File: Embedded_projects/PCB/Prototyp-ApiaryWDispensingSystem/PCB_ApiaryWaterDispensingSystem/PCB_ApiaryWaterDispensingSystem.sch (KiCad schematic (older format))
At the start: 0 parts

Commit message: added lot of changes to project #3
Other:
- note added: "Future"
- note added: "Ready"
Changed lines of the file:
@@
 $Descr A4 11693 8268
 encoding utf-8
-Sheet 1 7
+Sheet 1 9
 Title ""
 Date ""
@@
 $EndDescr
 $Sheet
-S 1180 1410 1050 1450
+S 4650 3150 1270 1660
 U 67C77D26
 F0 "Microcontroller_F4" 50
 F1 "microcontroller_F4.sch" 50
+F2 "SWO" B R 5920 4170 50
+F3 "USART_TX" O R 5920 4360 50
+F4 "USART_RX" I R 5920 4440 50
+F5 "TMS" B R 5920 4100 50
+F6 "TCK" B R 5920 4030 50
+F7 "MCO" B R 5920 4670 50
+F8 "NRST" B R 5920 4740 50
+F9 "BOOT0" B R 5920 4600 50
+F10 "SCL" B L 4650 4680 50
+F11 "SDA" B L 4650 4610 50
+F12 "B1_Button" O L 4650 3740 50
+F13 "B2_Button" O L 4650 3820 50
+F14 "B3_Button" O L 4650 3900 50
+F15 "B4_Button" O L 4650 3980 50
+F16 "SPI3_MOSI" O L 4650 3290 50
+F17 "SPI3_MISO" O L 4650 3360 50
+F18 "SPI3_CS" O L 4650 3440 50
+F19 "SPI3_SCK" O L 4650 3520 50
+F20 "APHASE" O R 5920 3300 50
+F21 "AENABLE" O R 5920 3370 50
+F22 "MODE" O R 5920 3450 50
 $EndSheet
 $Sheet
-S 5650 2000 1450 1350
+S 9410 1420 1450 1350
 U 67C77F5E
 F0 "MPPT" 50
@@
 $EndSheet
 $Sheet
-S 4200 3750 1100 1200
+S 2730 4410 1100 1200
 U 67D47B32
 F0 "sensors" 50
 F1 "sensors.sch" 50
-F2 "SDA" B L 4200 3950 50
-F3 "SCL" B L 4200 4050 50
+F2 "SDA" B R 3830 4610 50
+F3 "SCL" B R 3830 4680 50
+F4 "RST" B R 3830 5150 50
+F5 "BH_I2C_ADDR" B R 3830 5260 50
 $EndSheet
 $Sheet
-S 6100 3850 1150 1100
+S 6440 3100 1120 630
 U 67E19E2D
 F0 "sterownik_silnika" 50
 F1 "sterownik_silnika.sch" 50
-F2 "APHASE" I L 6100 4050 50
-F3 "BPHASE" I L 6100 4140 50
-F4 "AENBL" I L 6100 4230 50
-F5 "BENBL" I L 6100 4320 50
-F6 "MODE" I L 6100 4390 50
+F2 "APHASE" I L 6440 3300 50
+F3 "BPHASE" I L 6440 3510 50
+F4 "AENBL" I L 6440 3370 50
+F5 "BENBL" I L 6440 3580 50
+F6 "MODE" I L 6440 3440 50
 $EndSheet
 $Sheet
-S 7670 2200 1170 1120
+S 3220 2960 650  710
 U 67E3C70E
 F0 "SPI" 50
 F1 "SPI.sch" 50
+F2 "SPI3_SCK" I R 3870 3520 50
+F3 "SPI3_MOSI" I R 3870 3290 50
+F4 "SPI3_MISO" I R 3870 3360 50
+F5 "SPI3_CS" I R 3870 3440 50
 $EndSheet
 $Sheet
-S 3090 1680 900  1070
+S 7980 4040 970  510
+U 67F92507
+F0 "Zasilanie" 50
+F1 "Zasilanie.sch" 50
+F2 "PWR_ENn" I L 7980 4290 50
+$EndSheet
+Text Notes 9470 1070 0    157  ~ 0
+Future
+Text Notes 6670 3710 0    50   ~ 0
+Ready
+Text Notes 9810 1240 0    50   ~ 0
+Ready
+Wire Wire Line
+	4650 3290 3870 3290
+Wire Wire Line
+	3870 3360 4650 3360
+Wire Wire Line
+	3870 3440 4650 3440
+Wire Wire Line
+	3870 3520 4650 3520
+Wire Wire Line
+	3830 4610 4650 4610
+Wire Wire Line
+	4650 4680 3830 4680
+Wire Wire Line
+	7980 4290 7380 4290
+$Sheet
+S 1330 3540 800  620
+U 6823454A
+F0 "Buttons" 50
+F1 "Buttons.sch" 50
+F2 "UP_BUTTON" I R 2130 3740 50
+F3 "DOWN_BUTTON" I R 2130 3820 50
+F4 "ACTIVATED_BUTTON" I R 2130 3900 50
+F5 "OPTION_BUTTON" I R 2130 3980 50
+$EndSheet
+Wire Wire Line
+	4650 3740 2130 3740
+Wire Wire Line
+	2130 3820 4650 3820
+Wire Wire Line
+	4650 3900 2130 3900
+Wire Wire Line
+	2130 3980 4650 3980
+$Sheet
+S 6430 3920 900  1070
 U 6818B51C
 F0 "Microcontroller_F1" 50
 F1 "Microcontroller_F1.sch" 50
-F2 "STLK_TX" O L 3090 2280 50
-F3 "STLK_RX" I L 3090 2210 50
-F4 "MCO" U L 3090 2350 50
-F5 "PWR_ENn" O L 3090 2570 50
-F6 "NRST" O L 3090 1930 50
-F7 "TCK" O L 3090 2000 50
-F8 "TMS" O L 3090 2070 50
-F9 "SWO" O L 3090 2140 50
+F2 "STLK_TX" O L 6430 4530 50
+F3 "STLK_RX" I L 6430 4450 50
+F4 "MCO" U L 6430 4650 50
+F5 "PWR_ENn" O R 7330 4170 50
+F6 "NRST" O L 6430 4730 50
+F7 "TCK" O L 6430 4170 50
+F8 "TMS" O L 6430 4240 50
+F9 "SWO" O L 6430 4300 50
 $EndSheet
+Wire Wire Line
+	6440 3300 5920 3300
+Wire Wire Line
+	5920 3370 6440 3370
+Wire Wire Line
+	6440 3440 5950 3440
+Wire Wire Line
+	5950 3440 5950 3450
+Wire Wire Line
+	5950 3450 5920 3450
+Wire Wire Line
+	5920 4030 6220 4030
+Wire Wire Line
+	6220 4030 6220 4170
+Wire Wire Line
+	6220 4170 6430 4170
+Wire Wire Line
+	5920 4100 6160 4100
+Wire Wire Line
+	6160 4100 6160 4240
+Wire Wire Line
+	6160 4240 6430 4240
+Wire Wire Line
+	5920 4170 6100 4170
+Wire Wire Line
+	6100 4170 6100 4300
+Wire Wire Line
+	6100 4300 6430 4300
+Wire Wire Line
+	5920 4360 6250 4360
+Wire Wire Line
+	6250 4360 6250 4450
+Wire Wire Line
+	6250 4450 6430 4450
+Wire Wire Line
+	5920 4440 6180 4440
+Wire Wire Line
+	6180 4440 6180 4530
+Wire Wire Line
+	6180 4530 6430 4530
+Wire Wire Line
+	5920 4670 6340 4670
+Wire Wire Line
+	6340 4670 6340 4650
+Wire Wire Line
+	6340 4650 6430 4650
+Wire Wire Line
+	6430 4730 6170 4730
+Wire Wire Line
+	5960 4730 5960 4740
+Wire Wire Line
+	5960 4740 5920 4740
+Wire Wire Line
+	3830 5150 6170 5150
+Wire Wire Line
+	6170 5150 6170 4730
+Connection ~ 6170 4730
+Wire Wire Line
+	6170 4730 5960 4730
 $EndSCHEMATC

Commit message: Many design changes have been added over the past few months #3
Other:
- note added: "good"
- note removed: "Future"
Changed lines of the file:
@@
 $EndDescr
 $Sheet
-S 4650 3150 1270 1660
+S 4650 3150 1270 2080
 U 67C77D26
 F0 "Microcontroller_F4" 50
@@
 F5 "TMS" B R 5920 4100 50
 F6 "TCK" B R 5920 4030 50
-F7 "MCO" B R 5920 4670 50
-F8 "NRST" B R 5920 4740 50
-F9 "BOOT0" B R 5920 4600 50
-F10 "SCL" B L 4650 4680 50
-F11 "SDA" B L 4650 4610 50
+F7 "MCO" B R 5920 4615 50
+F8 "NRST" B R 5920 4695 50
+F9 "BOOT0" B R 5920 4545 50
+F10 "SCL" B L 4650 4965 50
+F11 "SDA" B L 4650 4875 50
 F12 "B1_Button" O L 4650 3740 50
 F13 "B2_Button" O L 4650 3820 50
@@
 F21 "AENABLE" O R 5920 3370 50
 F22 "MODE" O R 5920 3450 50
-$EndSheet
-$Sheet
-S 9410 1420 1450 1350
-U 67C77F5E
-F0 "MPPT" 50
-F1 "MPPT.sch" 50
-$EndSheet
-$Sheet
-S 2730 4410 1100 1200
+F23 "BENABLE" O R 5920 3585 50
+F24 "BPHASE" O R 5920 3520 50
+F25 "SQW" I L 4650 4795 50
+F26 "ADC1_IN0" I L 4650 5070 50
+F27 "SPI2_SCK" O L 4650 4155 50
+F28 "SPI2_MOSI" I L 4650 4235 50
+F29 "SPI2_MISO" I L 4650 4315 50
+F30 "SPI2_CS" I L 4650 4405 50
+F31 "BAT" I R 5920 5130 50
+F32 "VM" I R 5920 4985 50
+F33 "DC_DISPLAY" O L 4650 4560 50
+F34 "RST_DISPLAY" O L 4650 4645 50
+F35 "BACKLIGHT" O L 4650 4720 50
+$EndSheet
+$Sheet
+S 2040 5305 1100 1200
 U 67D47B32
 F0 "sensors" 50
 F1 "sensors.sch" 50
-F2 "SDA" B R 3830 4610 50
-F3 "SCL" B R 3830 4680 50
-F4 "RST" B R 3830 5150 50
-F5 "BH_I2C_ADDR" B R 3830 5260 50
+F2 "SDA" B R 3140 5505 50
+F3 "SCL" B R 3140 5575 50
+F4 "SQW" I R 3140 5385 50
+F5 "ADC1_IN0" I R 3140 5675 50
+F6 "BAT" I R 3140 5800 50
 $EndSheet
 $Sheet
@@
 F0 "Zasilanie" 50
 F1 "Zasilanie.sch" 50
-F2 "PWR_ENn" I L 7980 4290 50
-$EndSheet
-Text Notes 9470 1070 0    157  ~ 0
-Future
+F2 "PWR_ENn" I L 7980 4170 50
+F3 "VM" O L 7980 4260 50
+$EndSheet
 Text Notes 6670 3710 0    50   ~ 0
 Ready
-Text Notes 9810 1240 0    50   ~ 0
-Ready
 Wire Wire Line
 	4650 3290 3870 3290
@@
 Wire Wire Line
 	3870 3520 4650 3520
-Wire Wire Line
-	3830 4610 4650 4610
-Wire Wire Line
-	4650 4680 3830 4680
-Wire Wire Line
-	7980 4290 7380 4290
 $Sheet
 S 1330 3540 800  620
@@
 Wire Wire Line
 	2130 3980 4650 3980
+Wire Wire Line
+	6440 3300 5920 3300
+Wire Wire Line
+	5920 3370 6440 3370
+Wire Wire Line
+	6440 3440 5950 3440
+Wire Wire Line
+	5950 3440 5950 3450
+Wire Wire Line
+	5950 3450 5920 3450
+Wire Wire Line
+	5920 4030 6220 4030
+Wire Wire Line
+	6220 4030 6220 4170
+Wire Wire Line
+	6220 4170 6430 4170
+Wire Wire Line
+	5920 4100 6160 4100
+Wire Wire Line
+	6160 4100 6160 4240
+Wire Wire Line
+	6160 4240 6430 4240
+Wire Wire Line
+	5920 4170 6100 4170
+Wire Wire Line
+	6100 4170 6100 4300
+Wire Wire Line
+	6100 4300 6430 4300
+Wire Wire Line
+	5920 4360 6250 4360
+Wire Wire Line
+	6250 4360 6250 4450
+Wire Wire Line
+	6250 4450 6430 4450
+Wire Wire Line
+	5920 4440 6180 4440
+Wire Wire Line
+	6180 4440 6180 4530
+Wire Wire Line
+	6180 4530 6430 4530
+Wire Wire Line
+	7980 4170 7330 4170
+Text Notes 6740 5180 0    50   ~ 0
+good
+Text Notes 8290 4750 0    50   ~ 0
+good
+Text Notes 1650 4365 0    50   ~ 0
+good
+Wire Wire Line
+	6440 3510 5940 3510
+Wire Wire Line
+	5940 3510 5940 3520
+Wire Wire Line
+	5940 3520 5920 3520
+Wire Wire Line
+	5920 3585 6425 3585
+Wire Wire Line
+	6425 3585 6425 3580
+Wire Wire Line
+	6425 3580 6440 3580
+Text Notes 7680 3450 0    50   ~ 0
+good
+Text Notes 5145 3000 0    50   ~ 0
+good
+$Sheet
+S 2260 4120 885  970
+U 692A1EB2
+F0 "Display" 50
+F1 "Display.sch" 50
+F2 "SPI2_SCK" I R 3145 4200 50
+F3 "SPI2_MISO" I R 3145 4380 50
+F4 "SPI2_MOSI" I R 3145 4290 50
+F5 "SPI2_CS" I R 3145 4475 50
+F6 "DC_DISPLAY" I R 3145 4585 50
+F7 "RST_DISPLAY" I R 3145 4680 50
+F8 "BACKLIGHT" I R 3145 4770 50
+$EndSheet
 $Sheet
 S 6430 3920 900  1070
@@
 F2 "STLK_TX" O L 6430 4530 50
 F3 "STLK_RX" I L 6430 4450 50
-F4 "MCO" U L 6430 4650 50
+F4 "MCO" U L 6430 4660 50
 F5 "PWR_ENn" O R 7330 4170 50
 F6 "NRST" O L 6430 4730 50
@@
 $EndSheet
 Wire Wire Line
-	6440 3300 5920 3300
-Wire Wire Line
-	5920 3370 6440 3370
-Wire Wire Line
-	6440 3440 5950 3440
-Wire Wire Line
-	5950 3440 5950 3450
-Wire Wire Line
-	5950 3450 5920 3450
-Wire Wire Line
-	5920 4030 6220 4030
-Wire Wire Line
-	6220 4030 6220 4170
-Wire Wire Line
-	6220 4170 6430 4170
-Wire Wire Line
-	5920 4100 6160 4100
-Wire Wire Line
-	6160 4100 6160 4240
-Wire Wire Line
-	6160 4240 6430 4240
-Wire Wire Line
-	5920 4170 6100 4170
-Wire Wire Line
-	6100 4170 6100 4300
-Wire Wire Line
-	6100 4300 6430 4300
-Wire Wire Line
-	5920 4360 6250 4360
-Wire Wire Line
-	6250 4360 6250 4450
-Wire Wire Line
-	6250 4450 6430 4450
-Wire Wire Line
-	5920 4440 6180 4440
-Wire Wire Line
-	6180 4440 6180 4530
-Wire Wire Line
-	6180 4530 6430 4530
-Wire Wire Line
-	5920 4670 6340 4670
-Wire Wire Line
-	6340 4670 6340 4650
-Wire Wire Line
-	6340 4650 6430 4650
-Wire Wire Line
-	6430 4730 6170 4730
-Wire Wire Line
-	5960 4730 5960 4740
-Wire Wire Line
-	5960 4740 5920 4740
-Wire Wire Line
-	3830 5150 6170 5150
-Wire Wire Line
-	6170 5150 6170 4730
-Connection ~ 6170 4730
-Wire Wire Line
-	6170 4730 5960 4730
+	6430 4660 6010 4660
+Wire Wire Line
+	6010 4660 6010 4615
+Wire Wire Line
+	6010 4615 5920 4615
+Wire Wire Line
+	6390 4730 6430 4730
+Wire Wire Line
+	3465 4200 3145 4200
+Wire Wire Line
+	3145 4290 4305 4290
+Wire Wire Line
+	4305 4290 4305 4235
+Wire Wire Line
+	4305 4235 4650 4235
+Wire Wire Line
+	4650 4155 3465 4155
+Wire Wire Line
+	3465 4155 3465 4200
+Wire Wire Line
+	3145 4380 4425 4380
+Wire Wire Line
+	4425 4380 4425 4315
+Wire Wire Line
+	4425 4315 4650 4315
+Wire Wire Line
+	4650 4405 4460 4405
+Wire Wire Line
+	4460 4405 4460 4475
+Wire Wire Line
+	4460 4475 3145 4475
+Wire Wire Line
+	5920 4695 6390 4695
+Wire Wire Line
+	6390 4695 6390 4730
+Wire Wire Line
+	4305 5675 4305 5070
+Wire Wire Line
+	4305 5070 4650 5070
+Wire Wire Line
+	3140 5675 4305 5675
+Wire Wire Line
+	4650 4965 4185 4965
+Wire Wire Line
+	4185 4965 4185 5575
+Wire Wire Line
+	3140 5575 4185 5575
+Wire Wire Line
+	4070 5505 4070 4875
+Wire Wire Line
+	4070 4875 4650 4875
+Wire Wire Line
+	3140 5505 4070 5505
+Wire Wire Line
+	4650 4795 3960 4795
+Wire Wire Line
+	3960 4795 3960 5385
+Wire Wire Line
+	3140 5385 3960 5385
+Wire Wire Line
+	6040 5130 6040 5800
+Wire Wire Line
+	3140 5800 6040 5800
+Wire Wire Line
+	3145 4585 4450 4585
+Wire Wire Line
+	4450 4585 4450 4560
+Wire Wire Line
+	4450 4560 4650 4560
+Wire Wire Line
+	4650 4645 3225 4645
+Wire Wire Line
+	3225 4645 3225 4680
+Wire Wire Line
+	3225 4680 3145 4680
+Wire Wire Line
+	3145 4770 3280 4770
+Wire Wire Line
+	3280 4770 3280 4720
+Wire Wire Line
+	3280 4720 4650 4720
+Wire Wire Line
+	5920 5130 6040 5130
+Wire Wire Line
+	5920 4985 6175 4985
+Wire Wire Line
+	6175 4985 6175 5415
+Wire Wire Line
+	6175 5415 7620 5415
+Wire Wire Line
+	7620 5415 7620 4260
+Wire Wire Line
+	7620 4260 7980 4260
 $EndSCHEMATC

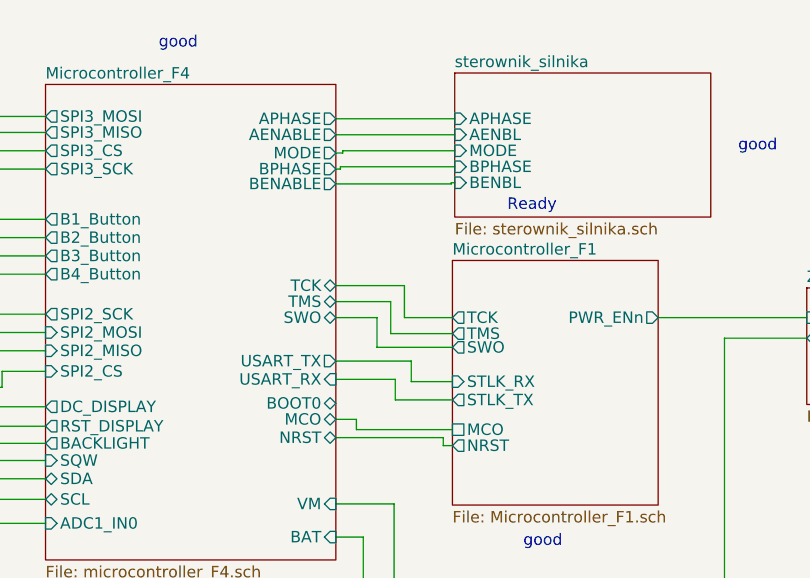
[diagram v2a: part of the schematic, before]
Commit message: All signal has been routed, the analog part needs to be completed
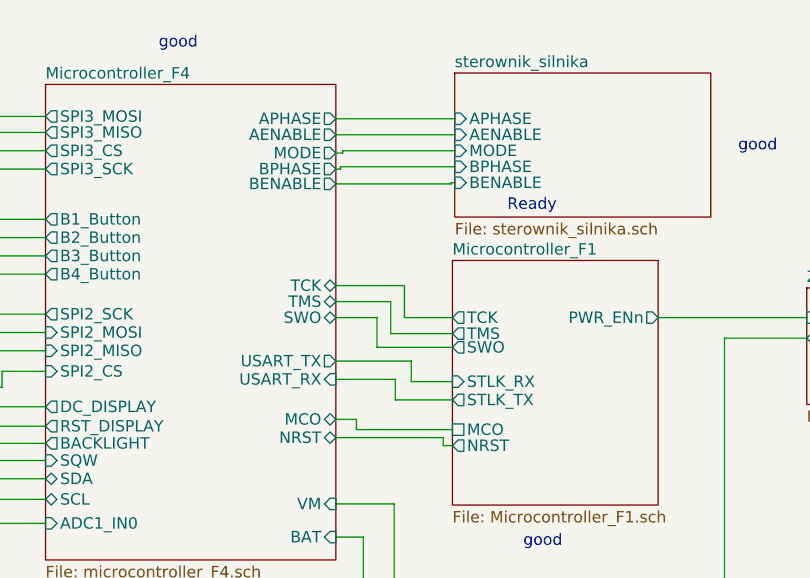
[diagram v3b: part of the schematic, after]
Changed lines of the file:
@@
 F7 "MCO" B R 5920 4615 50
 F8 "NRST" B R 5920 4695 50
-F9 "BOOT0" B R 5920 4545 50
-F10 "SCL" B L 4650 4965 50
-F11 "SDA" B L 4650 4875 50
-F12 "B1_Button" O L 4650 3740 50
-F13 "B2_Button" O L 4650 3820 50
-F14 "B3_Button" O L 4650 3900 50
-F15 "B4_Button" O L 4650 3980 50
-F16 "SPI3_MOSI" O L 4650 3290 50
-F17 "SPI3_MISO" O L 4650 3360 50
-F18 "SPI3_CS" O L 4650 3440 50
-F19 "SPI3_SCK" O L 4650 3520 50
-F20 "APHASE" O R 5920 3300 50
-F21 "AENABLE" O R 5920 3370 50
-F22 "MODE" O R 5920 3450 50
-F23 "BENABLE" O R 5920 3585 50
-F24 "BPHASE" O R 5920 3520 50
-F25 "SQW" I L 4650 4795 50
-F26 "ADC1_IN0" I L 4650 5070 50
-F27 "SPI2_SCK" O L 4650 4155 50
-F28 "SPI2_MOSI" I L 4650 4235 50
-F29 "SPI2_MISO" I L 4650 4315 50
-F30 "SPI2_CS" I L 4650 4405 50
-F31 "BAT" I R 5920 5130 50
-F32 "VM" I R 5920 4985 50
-F33 "DC_DISPLAY" O L 4650 4560 50
-F34 "RST_DISPLAY" O L 4650 4645 50
-F35 "BACKLIGHT" O L 4650 4720 50
+F9 "SCL" B L 4650 4965 50
+F10 "SDA" B L 4650 4875 50
+F11 "B1_Button" O L 4650 3740 50
+F12 "B2_Button" O L 4650 3820 50
+F13 "B3_Button" O L 4650 3900 50
+F14 "B4_Button" O L 4650 3980 50
+F15 "SPI3_MOSI" O L 4650 3290 50
+F16 "SPI3_MISO" O L 4650 3360 50
+F17 "SPI3_CS" O L 4650 3440 50
+F18 "SPI3_SCK" O L 4650 3520 50
+F19 "APHASE" O R 5920 3300 50
+F20 "AENABLE" O R 5920 3370 50
+F21 "MODE" O R 5920 3450 50
+F22 "BENABLE" O R 5920 3585 50
+F23 "BPHASE" O R 5920 3520 50
+F24 "SQW" I L 4650 4795 50
+F25 "ADC1_IN0" I L 4650 5070 50
+F26 "SPI2_SCK" O L 4650 4155 50
+F27 "SPI2_MOSI" I L 4650 4235 50
+F28 "SPI2_MISO" I L 4650 4315 50
+F29 "SPI2_CS" I L 4650 4405 50
+F30 "BAT" I R 5920 5130 50
+F31 "VM" I R 5920 4985 50
+F32 "DC_DISPLAY" O L 4650 4560 50
+F33 "RST_DISPLAY" O L 4650 4645 50
+F34 "BACKLIGHT" O L 4650 4720 50
 $EndSheet
 $Sheet
@@
 F2 "APHASE" I L 6440 3300 50
 F3 "BPHASE" I L 6440 3510 50
-F4 "AENBL" I L 6440 3370 50
-F5 "BENBL" I L 6440 3580 50
-F6 "MODE" I L 6440 3440 50
+F4 "MODE" I L 6440 3440 50
+F5 "AENABLE" I L 6440 3370 50
+F6 "BENABLE" I L 6440 3580 50
 $EndSheet
 $Sheet
